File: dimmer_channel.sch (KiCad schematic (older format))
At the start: 53 parts, among them J3 Conn_01x05_Male, Q1 S9013, Q10 BSS84, Q11 2N7002, Q12 BSS84, Q13 VS5810AS, Q14 VS5810AS, Q15 VS5810AS, Q16 VS5810AS, Q2 BSS84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

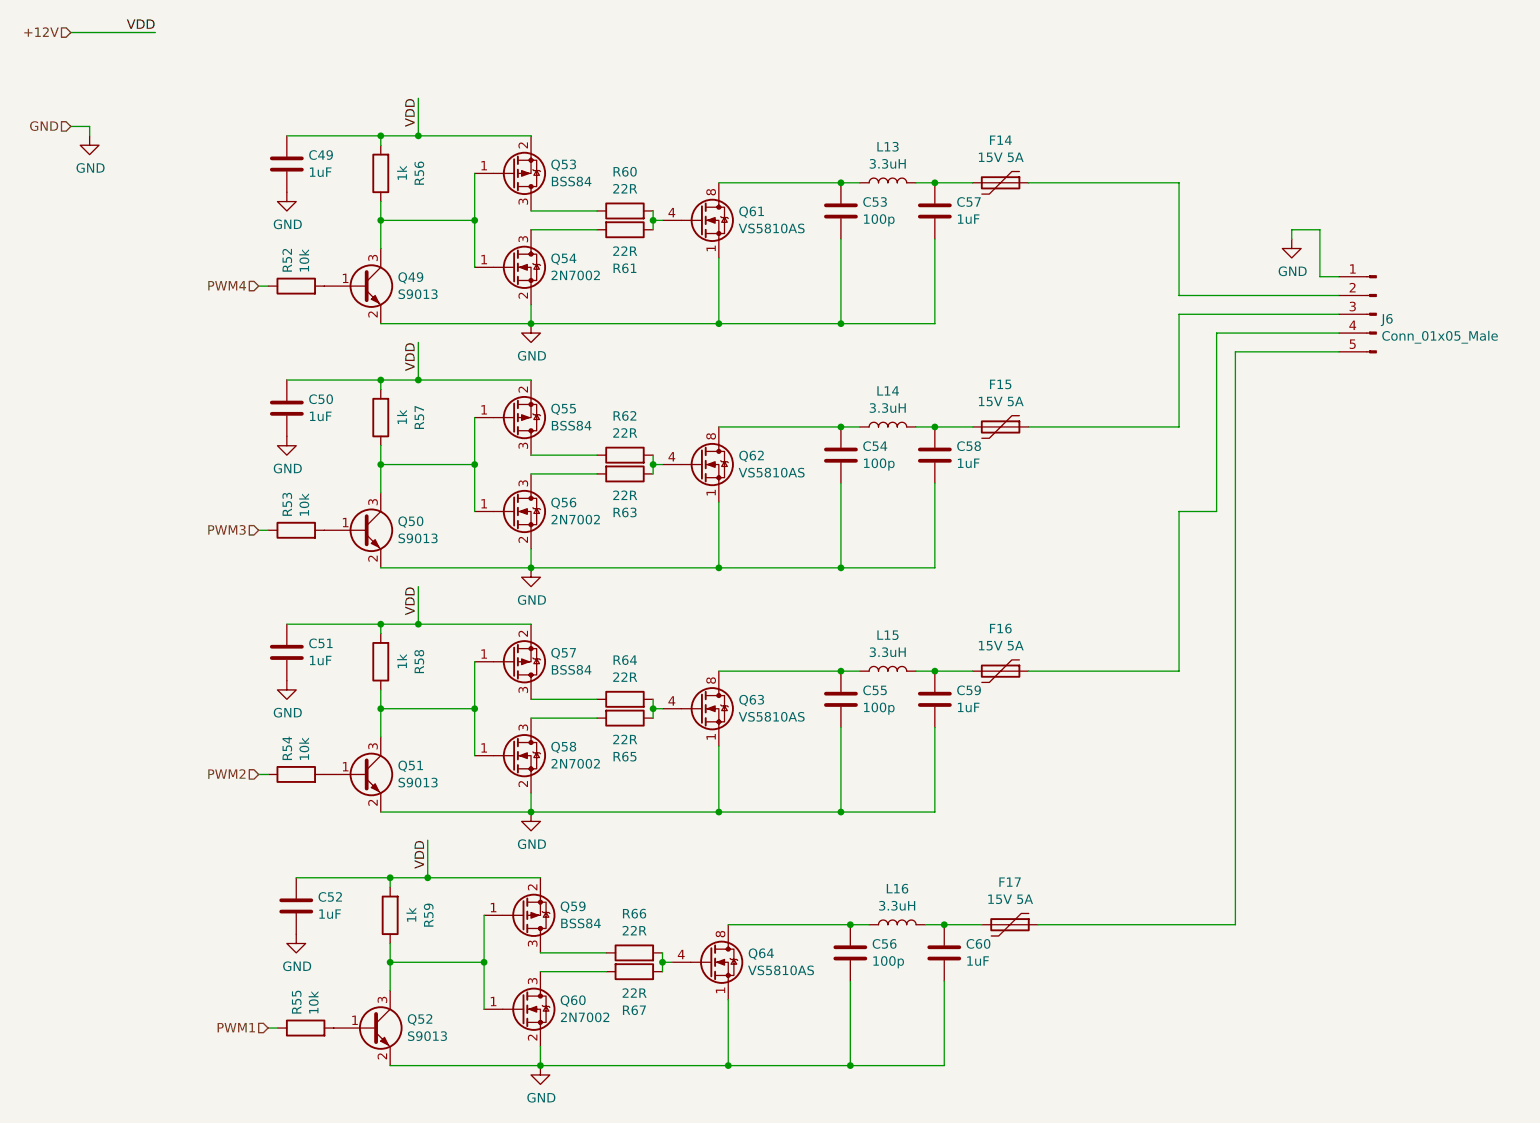
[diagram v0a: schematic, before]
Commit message: Add metadata to schematic
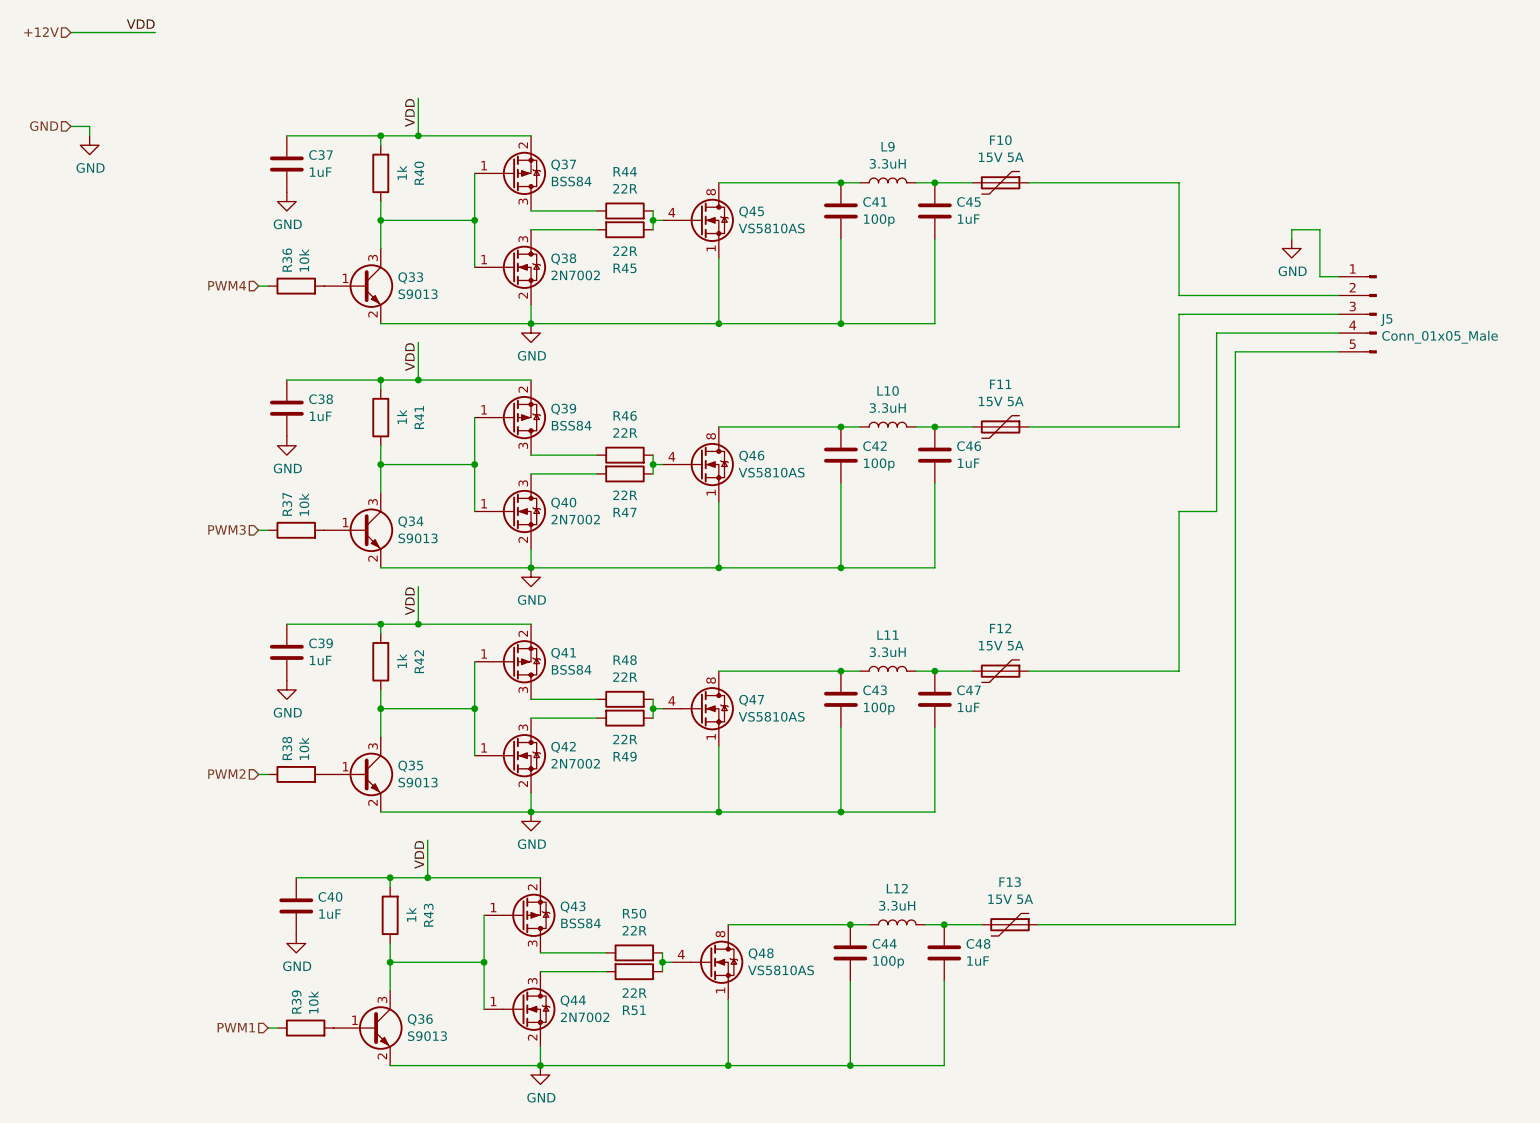
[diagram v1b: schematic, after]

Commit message: Add tooling holes
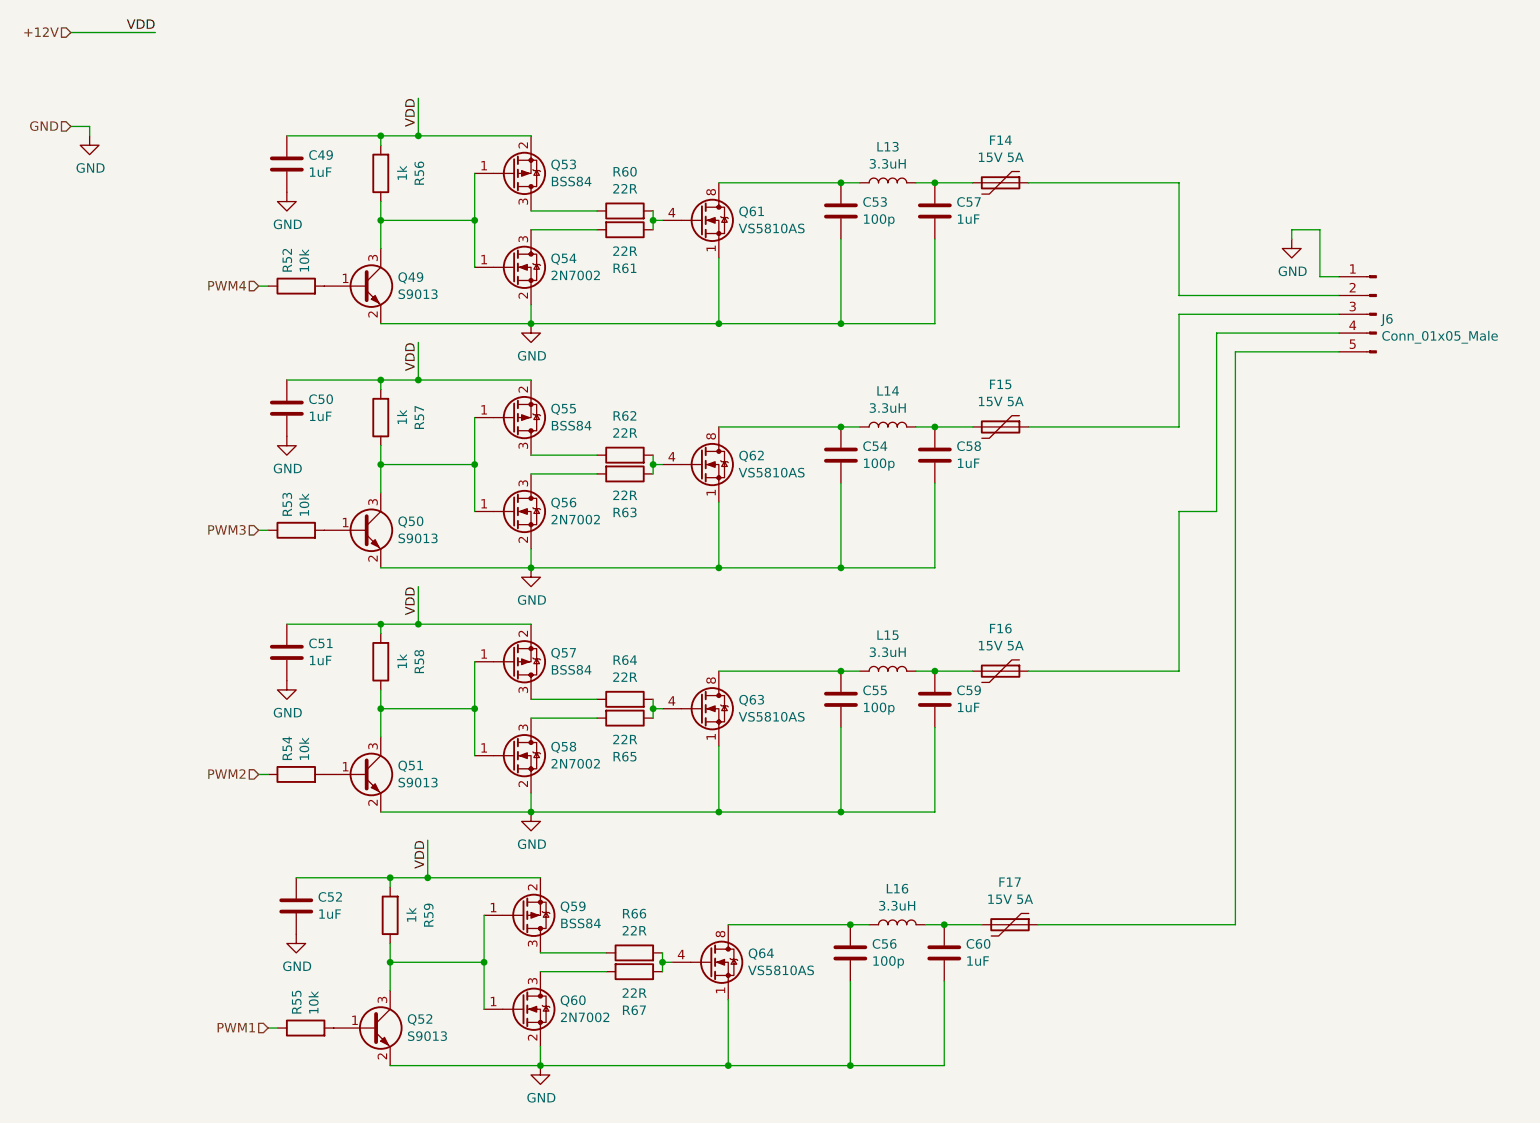
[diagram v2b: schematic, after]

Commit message: Change inductor to 4.7uH for JLC assembly
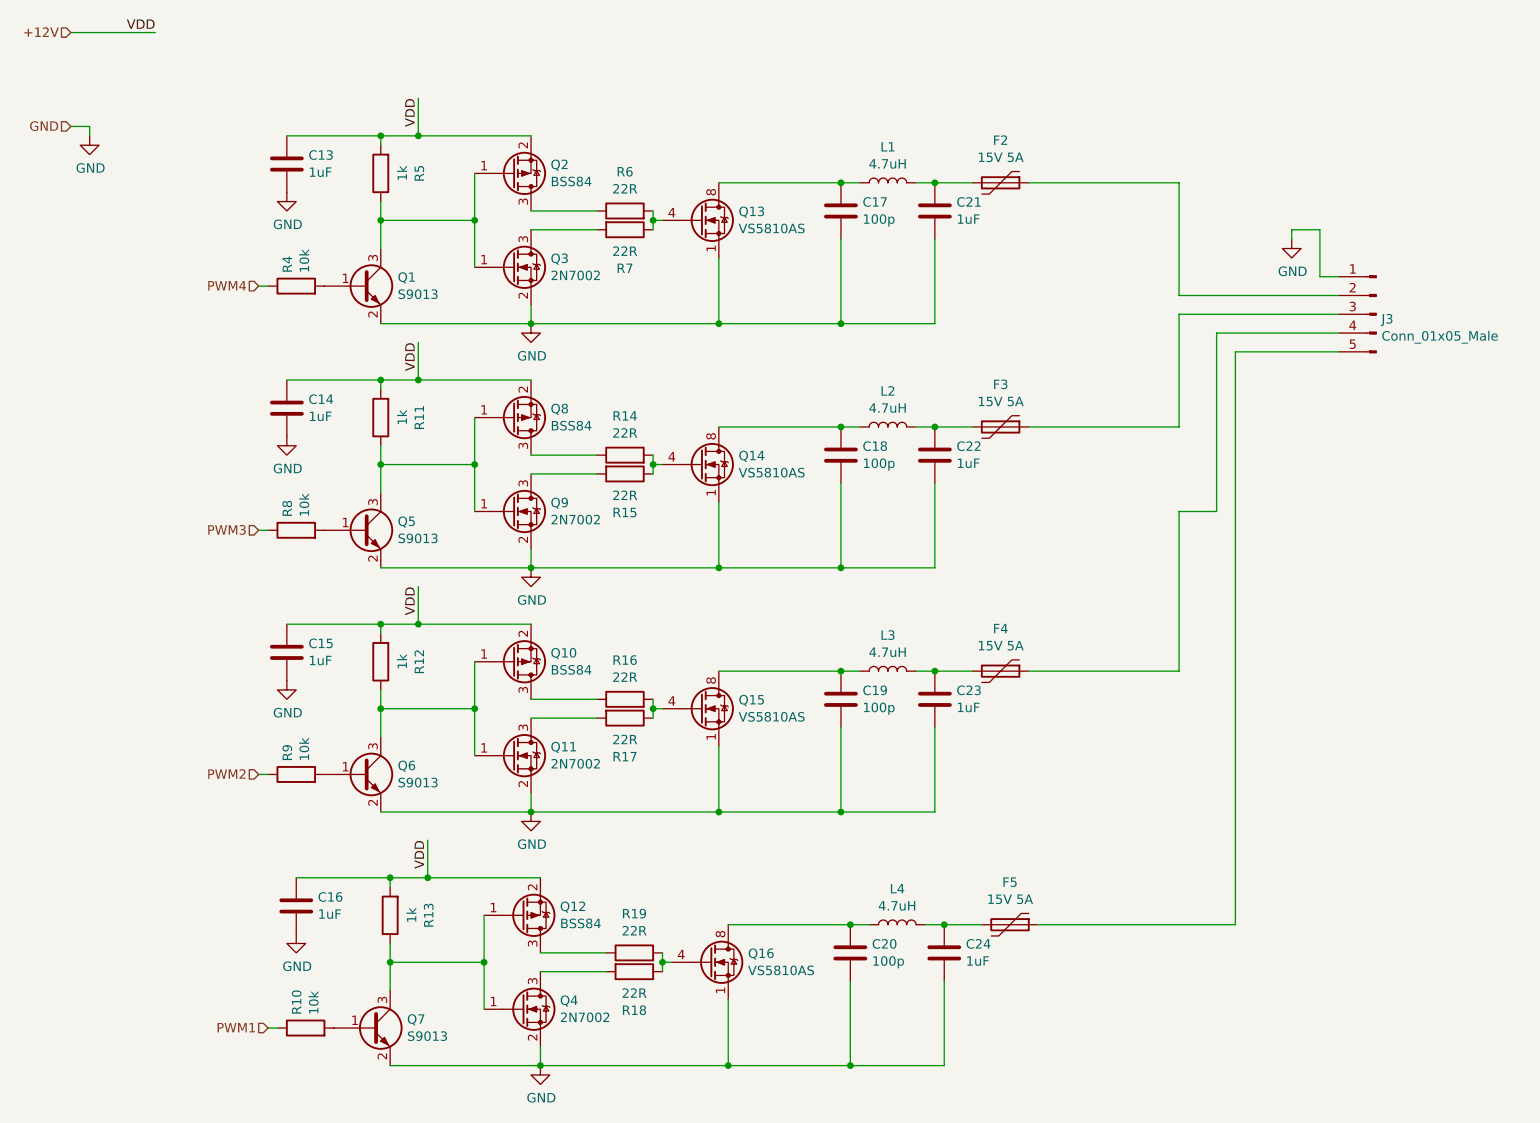
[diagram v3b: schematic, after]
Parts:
- L1, L2, L3, L4: value 3.3uH -> 4.7uH; LCSC C143963 -> C183899

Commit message: Fix 1206 component with 0603 LCSC part number (1uF cap)
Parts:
- C24: LCSC C15849 -> C1848
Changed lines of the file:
@@
 	1    0    0    -1
 $EndComp
-Connection ~ 5900 5550
-Wire Wire Line
-	6100 5550 5900 5550
 $Comp
 L Device:Polyfuse F5
@@
 Wire Wire Line
 	5500 5550 5400 5550
-Wire Wire Line
-	5900 5550 5800 5550
 Connection ~ 5400 6300
 Wire Wire Line
@@
 Wire Wire Line
 	5900 5850 5900 6300
-$Comp
-L Device:C C24
-U 1 1 5EBED575
-P 5900 5700
-AR Path="/5EADE2DF/5EBED575" Ref="C24"  Part="1"
-AR Path="/5EAEA785/5EBED575" Ref="C36"  Part="1"
-AR Path="/5EAEB6DE/5EBED575" Ref="C48"  Part="1"
-AR Path="/5EAEC5FF/5EBED575" Ref="C60"  Part="1"
-F 0 "C24" H 6015 5746 50  0000 L CNN
-F 1 "1uF" H 6015 5655 50  0000 L CNN
-F 2 "Capacitor_SMD:C_1206_3216Metric" H 5938 5550 50  0001 C CNN
-F 3 "~" H 5900 5700 50  0001 C CNN
-F 4 "C15849" H 5900 5700 50  0001 C CNN "LCSC"
-	1    5900 5700
-	1    0    0    -1
-$EndComp
 Wire Wire Line
 	5400 5550 4750 5550
@@
 Wire Wire Line
 	3150 5300 3750 5300
+Connection ~ 5900 5550
+Wire Wire Line
+	6100 5550 5900 5550
+Wire Wire Line
+	5900 5550 5800 5550
+$Comp
+L Device:C C24
+U 1 1 5EBED575
+P 5900 5700
+AR Path="/5EADE2DF/5EBED575" Ref="C24"  Part="1"
+AR Path="/5EAEA785/5EBED575" Ref="C36"  Part="1"
+AR Path="/5EAEB6DE/5EBED575" Ref="C48"  Part="1"
+AR Path="/5EAEC5FF/5EBED575" Ref="C60"  Part="1"
+F 0 "C24" H 6015 5746 50  0000 L CNN
+F 1 "1uF" H 6015 5655 50  0000 L CNN
+F 2 "Capacitor_SMD:C_1206_3216Metric" H 5938 5550 50  0001 C CNN
+F 3 "~" H 5900 5700 50  0001 C CNN
+F 4 "C1848" H 5900 5700 50  0001 C CNN "LCSC"
+	1    5900 5700
+	1    0    0    -1
+$EndComp
 $EndSCHEMATC
